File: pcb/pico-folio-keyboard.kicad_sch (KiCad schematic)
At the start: 133 parts, among them SW1 SW_Push, SW10 SW_Push, SW11 SW_Push, SW12 SW_Push, SW13 SW_Push, SW14 SW_Push, SW15 SW_Push, SW16 SW_Push, SW17 SW_Push, SW18 SW_Push, SW19 SW_Push, SW2 SW_Push, SW20 SW_Push, SW21 SW_Push, SW22 SW_Push, SW23 SW_Push, SW24 SW_Push, SW25 SW_Push, SW26 SW_Push, SW27 SW_Push, SW28 SW_Push, SW29 SW_Push, SW3 SW_Push, SW30 SW_Push, SW31 SW_Push, SW32 SW_Push, SW33 SW_Push, SW34 SW_Push, SW35 SW_Push, SW36 SW_Push, SW37 SW_Push, SW38 SW_Push, SW39 SW_Push, SW4 SW_Push, SW40 SW_Push, SW41 SW_Push, SW42 SW_Push, SW43 SW_Push, SW44 SW_Push, SW45 SW_Push, SW46 SW_Push, SW47 SW_Push, SW48 SW_Push, SW49 SW_Push, SW5 SW_Push, SW50 SW_Push, SW51 SW_Push, SW52 SW_Push, SW53 SW_Push, SW54 SW_Push, SW55 SW_Push, SW56 SW_Push, SW57 SW_Push, SW58 SW_Push, SW59 SW_Push, SW6 SW_Push, SW60 SW_Push, SW61 SW_Push, SW62 SW_Push, SW63 SW_Push, SW64 SW_Push, SW7 SW_Push, SW8 SW_Push, SW9 SW_Push

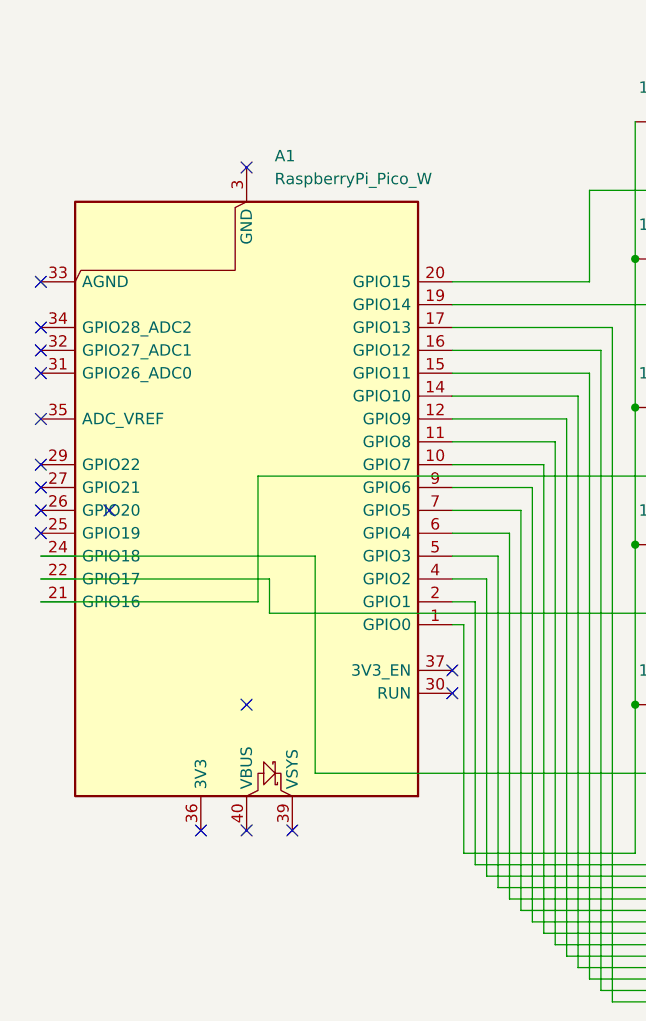
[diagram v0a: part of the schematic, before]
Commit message: updated schematic and pcb to break out vbus and gnd for usb without bodge wires
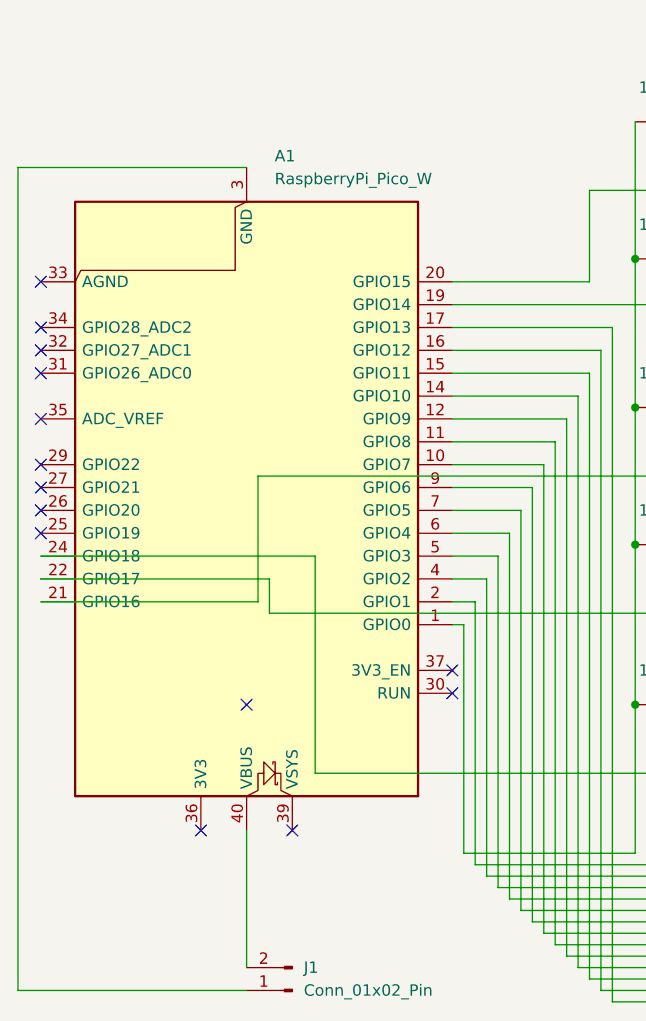
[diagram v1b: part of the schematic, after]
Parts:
- added J1: Conn_01x02_Pin, Connector_PinHeader_2.54mm:PinHeader_1x02_P2.54mm_Vertical, symbol Connector:Conn_01x02_Pin
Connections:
- net at A1.13 (GND), A1.18 (GND), A1.23 (GND)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: now also J1.1 (Pin_1)
- net at A1.40 (VBUS): now also J1.2 (Pin_2)
- no-connect marks 87 -> 84
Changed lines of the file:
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@@
 	)
 	(no_connect
-		(at 39.37 143.51)
-	)
-	(no_connect
 		(at 330.2 67.31)
 	)
@@
 	)
 	(no_connect
-		(at 39.37 69.85)
-	)
-	(no_connect
 		(at 262.89 82.55)
 	)
@@
 		(at 405.13 99.06)
 	)
-	(no_connect
-		(at 24.13 107.95)
-	)
 	(wire
 		(pts
@@
 	(wire
 		(pts
+			(xy 39.37 69.85) (xy 13.97 69.85)
+		)
+		(stroke
+			(width 0)
+			(type default)
+		)
+	)
+	(wire
+		(pts
 			(xy 184.15 111.76) (xy 184.15 114.3)
 		)
@@
 	(wire
 		(pts
+			(xy 13.97 69.85) (xy 13.97 161.29)
+		)
+		(stroke
+			(width 0)
+			(type default)
+		)
+	)
+	(wire
+		(pts
 			(xy 90.17 80.01) (xy 90.17 82.55)
 		)
@@
 	(wire
 		(pts
+			(xy 13.97 161.29) (xy 39.37 161.29)
+		)
+		(stroke
+			(width 0)
+			(type default)
+		)
+	)
+	(wire
+		(pts
 			(xy 168.91 104.14) (xy 181.61 104.14)
 		)
@@
 	(wire
 		(pts
+			(xy 39.37 143.51) (xy 39.37 158.75)
+		)
+		(stroke
+			(width 0)
+			(type default)
+		)
+	)
+	(wire
+		(pts
 			(xy 330.2 87.63) (xy 342.9 87.63)
 		)
@@
 					(unit 1)
 				)
+			)
+		)
+	)
+	(symbol
+		(lib_id "Connector:Conn_01x02_Pin")
+		(at 44.45 161.29 180)
+		(unit 1)
+		(exclude_from_sim no)
+		(in_bom yes)
+		(on_board yes)
+		(dnp no)
+		(fields_autoplaced yes)
+		(property "Reference" "J1"
+			(at 45.72 158.7499 0)
+			(effects
+				(font
+					(size 1.27 1.27)
+				)
+				(justify right)
+			)
+		)
+		(property "Value" "Conn_01x02_Pin"
+			(at 45.72 161.2899 0)
+			(effects
+				(font
+					(size 1.27 1.27)
+				)
+				(justify right)
+			)
+		)
+		(property "Footprint" "Connector_PinHeader_2.54mm:PinHeader_1x02_P2.54mm_Vertical"
+			(at 44.45 161.29 0)
+			(effects
+				(font
+					(size 1.27 1.27)
+				)
+				(hide yes)
+			)
+		)
+		(property "Datasheet" "~"
+			(at 44.45 161.29 0)
+			(effects
+				(font
+					(size 1.27 1.27)
+				)
+				(hide yes)
+			)
+		)
+		(property "Description" "Generic connector, single row, 01x02, script generated"
+			(at 44.45 161.29 0)
+			(effects
+				(font
+					(size 1.27 1.27)
+				)
+				(hide yes)
+			)
+		)
+		(pin "1"
+		)
+		(pin "2"
+		)
+		(instances
+			(project ""
+				(path "/0c313c10-1649-499e-9cc1-bdc2360ef474"
+					(reference "J1")
+					(unit 1)
+				)
